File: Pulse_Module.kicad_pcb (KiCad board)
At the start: 2 copper layers, 124.8 x 83.6 mm, 68 parts, among them CON1 AVR-ISP-10, CON2 AVR-JTAG-10, CON3 BARREL_JACK, IC1 ATMEGA1280-A, P1 CONN_02X20, P2 USB_OTG, P3 CONN_01X03, P4 CONN_01X03, SW1 SW_PUSH, U1 74HCT541_PWR, U2 PL2303, U3 AMS1117, U6 WS2812, U7 WS2812, U8 WS2812, X1 CRYSTAL, Y1 CRYSTAL

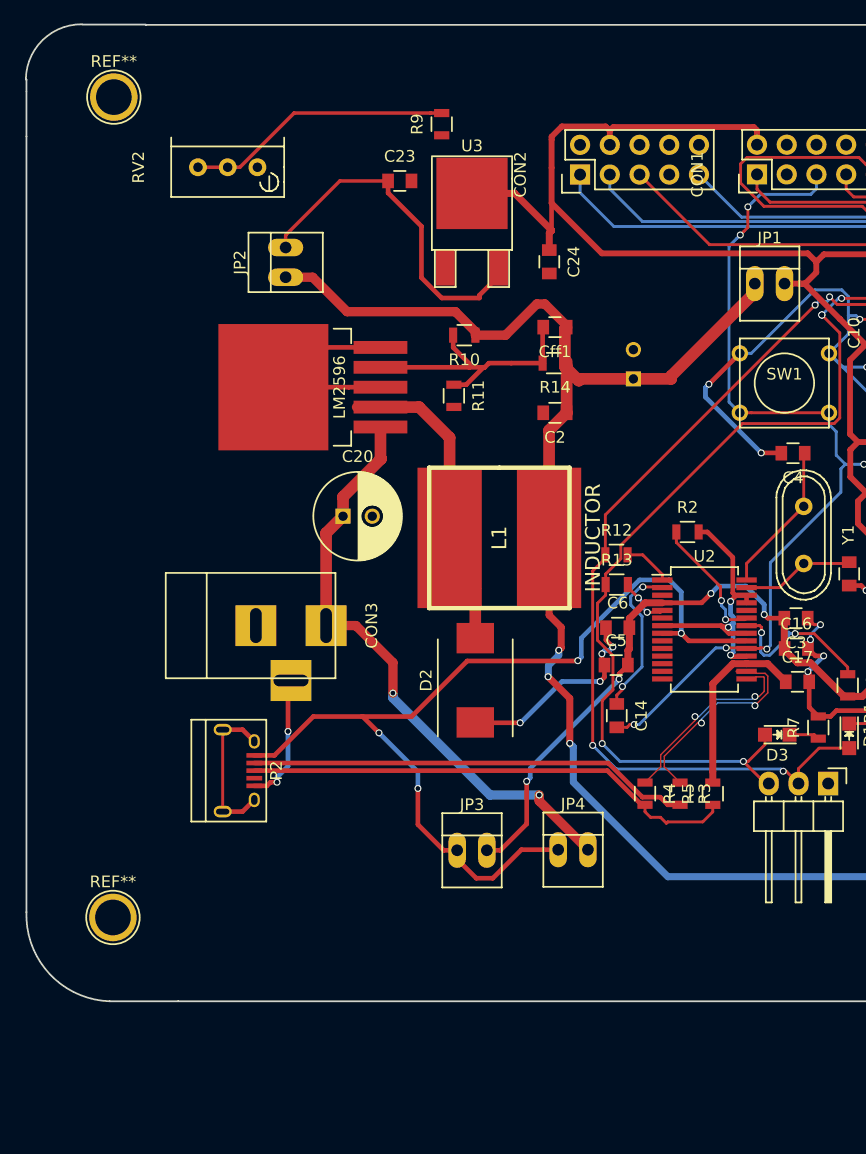
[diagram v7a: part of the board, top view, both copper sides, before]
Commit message: перенесён футпринт С1 вперёд
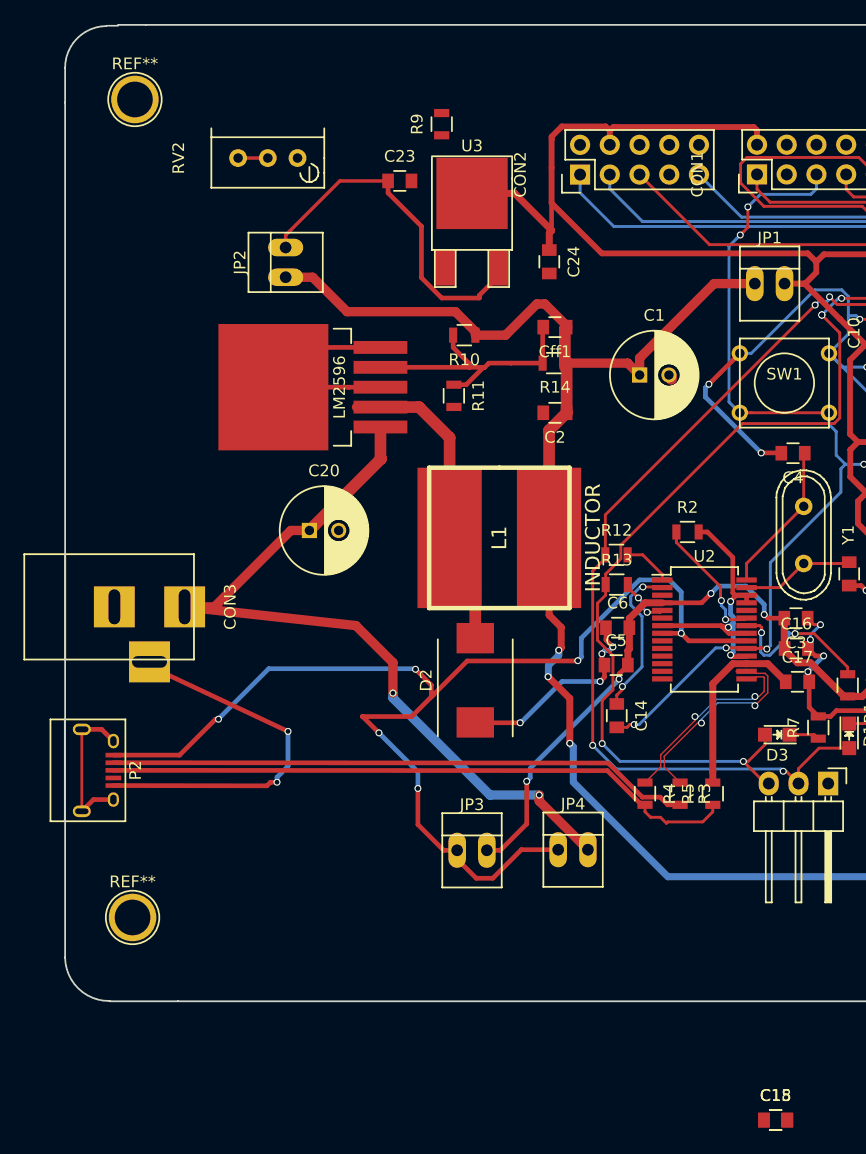
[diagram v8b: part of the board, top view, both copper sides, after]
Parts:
- added C15, C18: 0.1uF, Capacitors_SMD:C_0805, F.Cu at (151.4, 167.9)
- C1: moved to F.Cu
- moved CON3 12.2 mm to (94.7, 124.0)
- moved P2 12.0 mm to (93.2, 138.0)
- moved RV2 3.52 mm to (110.5, 85.7)
- moved C20 3.12 mm to (111.6, 117.5)
- moved REF** 1.81 mm to (96.6, 80.7)
- moved REF** 1.68 mm to (96.4, 150.6)
- moved C1 0.63 mm to (139.8, 104.2), turned to 0 degrees
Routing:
- net GND: track 344.2 -> 365.7 mm
- net USB_IN: track 81.6 -> 103.2 mm, vias 4 -> 6
- net Net-(R9-Pad2): track 22.7 -> 2.54 mm
- net /Sheet56D88A8D/Vin: track 51.4 -> 69.4 mm
- net Net-(P2-Pad3): track 42.4 -> 54.4 mm
- net Net-(P2-Pad2): track 37.9 -> 49.9 mm
- net /Sheet56DEE0DD/Vcc: track 163.6 -> 164.3 mm
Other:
- board size 124.8 x 83.6 mm -> 121.4 x 83.5 mm
